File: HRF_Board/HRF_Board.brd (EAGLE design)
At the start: 11 x 13.8 mm, 7 parts, among them U1 MAX30101EFD

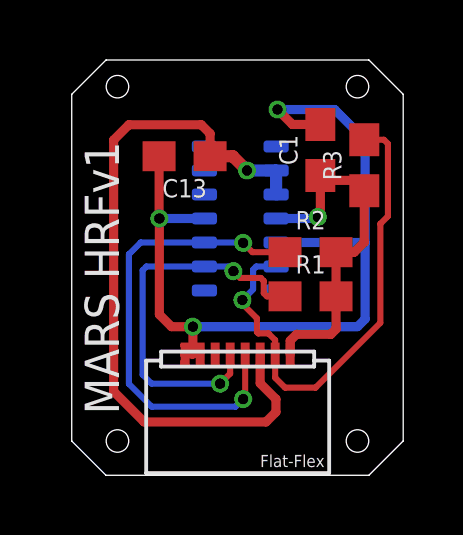
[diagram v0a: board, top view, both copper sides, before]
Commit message: Rerouted with new connector and added full ground plane
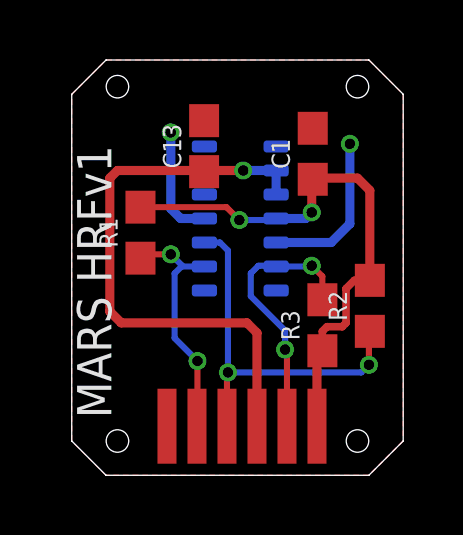
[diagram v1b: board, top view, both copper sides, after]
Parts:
- removed U$9: FLAT_FLEX_8, FLAT_FLEX:FLAT_FLEX_8
- added U$1: HRF_CONN, HRF_CONN:HRF_CONN
- moved R1 6.05 mm to (2.29, 8.09), turned to 90 degrees
- moved R3 5.51 mm to (8.35, 5.00)
- moved R2 2.67 mm to (9.94, 5.65), turned to 90 degrees
- moved C13 0.73 mm to (4.41, 11.0), turned to 90 degrees
- moved C1 0.28 mm to (8.03, 10.7)
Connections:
- net 1.8V: now also U$1.P$6; no longer U$9.8
- net 3.3V: now also U$1.P$4; no longer U$9.6
- net GND: now also U$1.P$1; no longer U$9.1, U$9.2
- net HR_SCL: now also U$1.P$2; no longer U$9.4
- net HR_SDA: now also U$1.P$3; no longer U$9.5
- net INT: now also U$1.P$5; no longer U$9.7
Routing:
- net GND: track 28.8 -> 9.18 mm, vias 3 -> 2
- net INT: track 16.7 -> 9.03 mm, vias 1 -> 2
- net 1.8V: track 12.0 -> 18.4 mm, vias 1 -> 2
- net 3.3V: track 24.0 -> 19.2 mm
- net HR_SCL: track 12.7 -> 8.13 mm
- net HR_SDA: track 15.6 -> 12.7 mm
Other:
- board text removed: "Jacob Bobson"
